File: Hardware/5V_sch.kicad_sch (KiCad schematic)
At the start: 19 parts, among them IC2 TPS563200DDCR

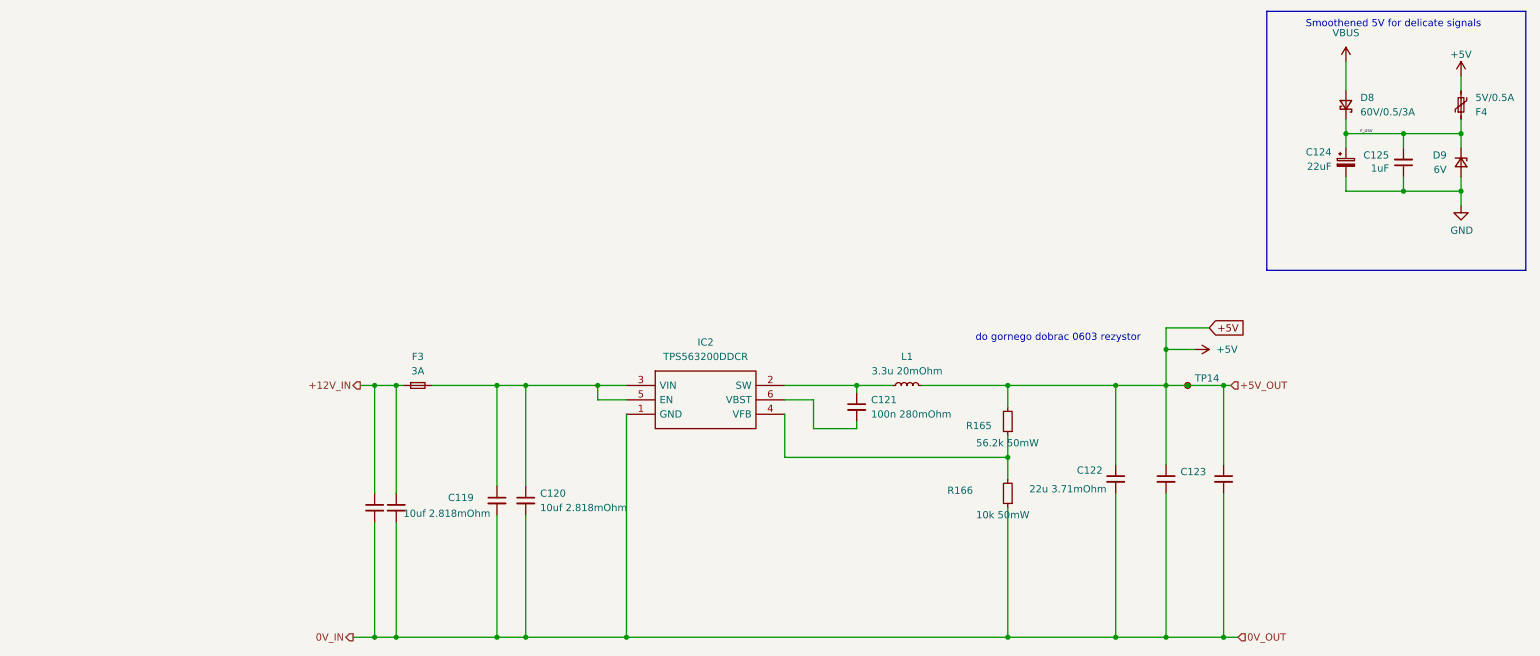
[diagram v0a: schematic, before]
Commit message: Dodano diody TVS na każdej części zasilania, zmieniono bezpieczniki, podzielono bezpieczniki na bezpieczniki do prądów wewnętrznych oraz zewnętrznych,poprawiono małe błedy
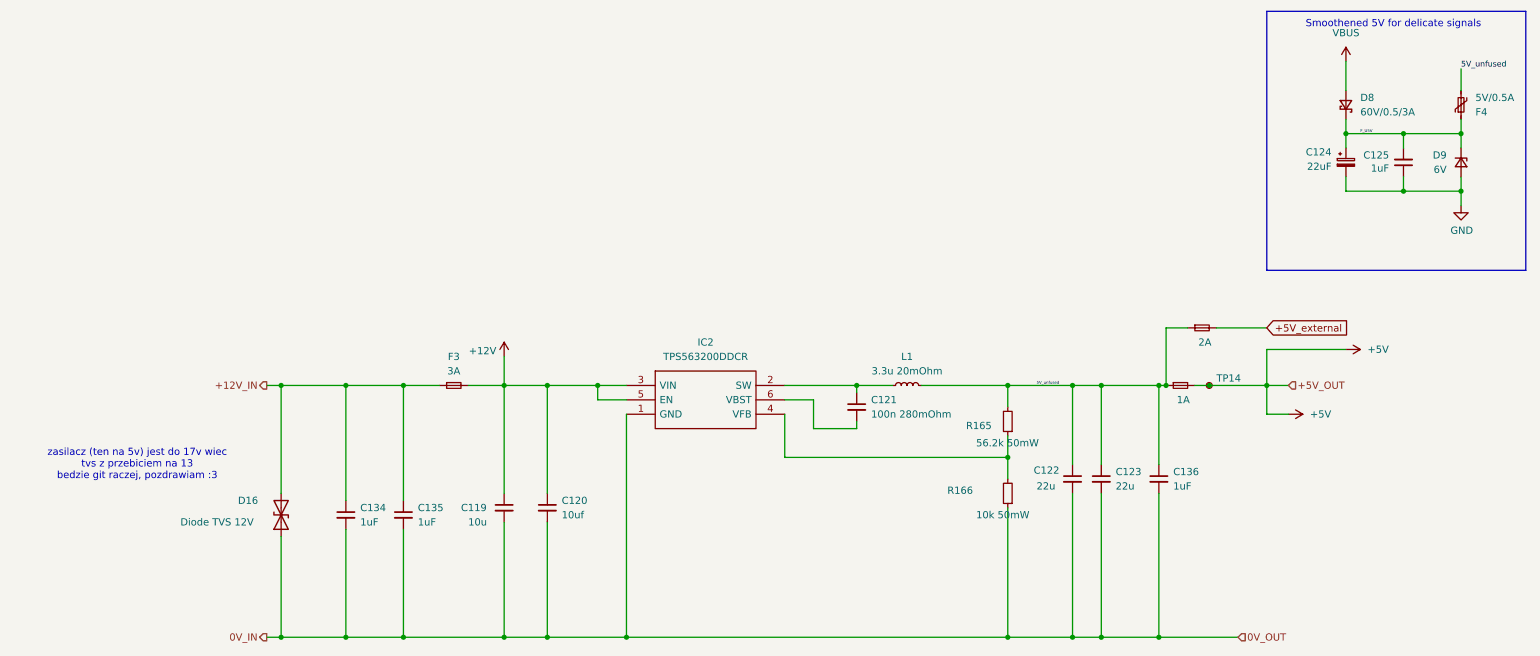
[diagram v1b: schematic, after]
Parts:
- added D16: Diode TVS 12V, Diode_SMD:D_SOD-323F, symbol Device:D_TVS
- added F2: 1A, Fuse:Fuse_0603_1608Metric_Pad1.05x0.95mm_HandSolder, symbol Device:Fuse_Small
- added F6: 2A, Fuse:Fuse_0603_1608Metric_Pad1.05x0.95mm_HandSolder, symbol Device:Fuse_Small
- C119: value 10uf 2.818mOhm -> 10u
- C120: value 10uf 2.818mOhm -> 10uf
- C122, C123: value 22u 3.71mOhm -> 22u; Field5 (none) -> 22u 3.71mOhm
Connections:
- net +12V_IN: now also D16.2 (A2)
- net +5V: now also F2.2; no longer C122.1, C123.1, C136.1, F4.2, L1.2, R165.2
- net 0V_IN: now also D16.1 (A1)
- net +12V: now reaches C119.1, C120.1, F3.2, IC2.3 (VIN), IC2.5 (EN)
- new net +5V_external: F6.2
- new net 5V_unfused: C122.1, C123.1, C136.1, F2.1, F4.2, F6.1, L1.2, R165.2
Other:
- note added: "zasilacz (ten na 5v) jest do 17v wiec tvs z przebiciem na 13 bedzie git raczej, pozdrawiam :3"
- note removed: "do gornego dobrac 0603 rezystor"
- moved on the sheet: C119, C120, C122, C123, F3, TP14

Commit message: Wiecej zmian wizualnych pod produkcje
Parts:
- added TP12: TestPoint_Small, TestPoint:TestPoint_Pad_D1.0mm, symbol Connector:TestPoint_Small
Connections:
- net +12V: now also TP12.1
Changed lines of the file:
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@@
+	)
+	(junction
+		(at 106.68 82.55)
+		(diameter 0)
+		(color 0 0 0 0)
 	)
 	(junction
@@
 	(wire
 		(pts
+			(xy 106.68 82.55) (xy 110.49 82.55)
+		)
+		(stroke
+			(width 0)
+			(type default)
+		)
+	)
+	(wire
+		(pts
 			(xy 218.44 82.55) (xy 219.71 82.55)
 		)
@@
 	(wire
 		(pts
-			(xy 102.87 82.55) (xy 110.49 82.55)
+			(xy 102.87 82.55) (xy 106.68 82.55)
 		)
 		(stroke
@@
 					(unit 1)
 				)
+			)
+		)
+	)
+	(symbol
+		(lib_id "Connector:TestPoint_Small")
+		(at 106.68 82.55 0)
+		(unit 1)
+		(exclude_from_sim no)
+		(in_bom yes)
+		(on_board yes)
+		(dnp no)
+		(fields_autoplaced yes)
+		(property "Reference" "TP12"
+			(at 107.95 81.2799 0)
+			(effects
+				(font
+					(size 1.27 1.27)
+				)
+				(justify left)
+			)
+		)
+		(property "Value" "TestPoint_Small"
+			(at 107.95 83.8199 0)
+			(effects
+				(font
+					(size 1.27 1.27)
+				)
+				(justify left)
+				(hide yes)
+			)
+		)
+		(property "Footprint" "TestPoint:TestPoint_Pad_D1.0mm"
+			(at 111.76 82.55 0)
+			(effects
+				(font
+					(size 1.27 1.27)
+				)
+				(hide yes)
+			)
+		)
+		(property "Datasheet" "~"
+			(at 111.76 82.55 0)
+			(effects
+				(font
+					(size 1.27 1.27)
+				)
+				(hide yes)
+			)
+		)
+		(property "Description" "test point"
+			(at 106.68 82.55 0)
+			(effects
+				(font
+					(size 1.27 1.27)
+				)
+				(hide yes)
+			)
+		)
+		(pin "1"
+		)
+		(instances
+			(project "BMS"
+				(path "/26289bb6-56bc-4ca1-b1a2-18d58d1afdf5/b306fb08-ef5e-4bf5-8efa-c4e5200f566a/3120d456-738f-4dcb-b831-006287d4ee74"
+					(reference "TP12")
+					(unit 1)
+				)

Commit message: zmiany w kodzier bq
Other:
- note removed: "zasilacz (ten na 5v) jest do 17v wiec tvs z przebiciem na 13 bedzie git raczej, pozdrawiam :3"
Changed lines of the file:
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@@
-		)
-	)
-	(text "zasilacz (ten na 5v) jest do 17v wiec \ntvs z przebiciem na 13 \nbedzie git raczej, pozdrawiam :3\n"
-		(exclude_from_sim no)
-		(at 38.1 96.52 0)
-		(effects
-			(font
-				(size 1.27 1.27)
-			)
 		)
 	)
